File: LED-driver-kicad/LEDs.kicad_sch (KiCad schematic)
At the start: 13 parts, among them Q1 2N7002K, U2 MIC3205YML-TR

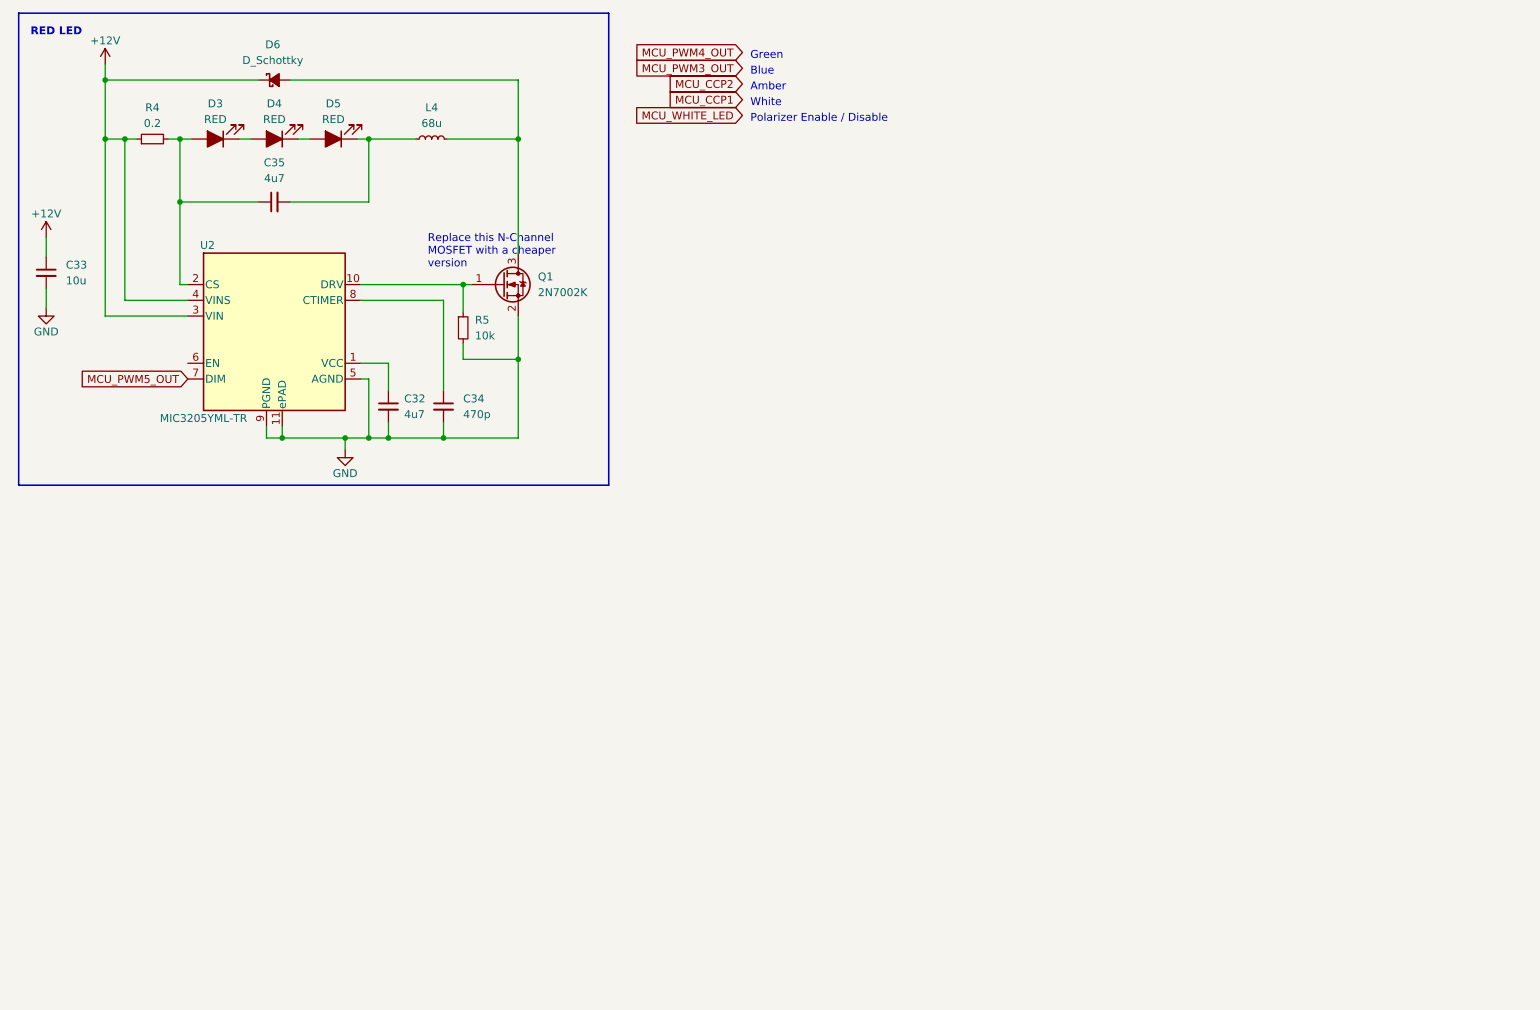
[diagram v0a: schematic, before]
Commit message: update RGB LED driver circuits
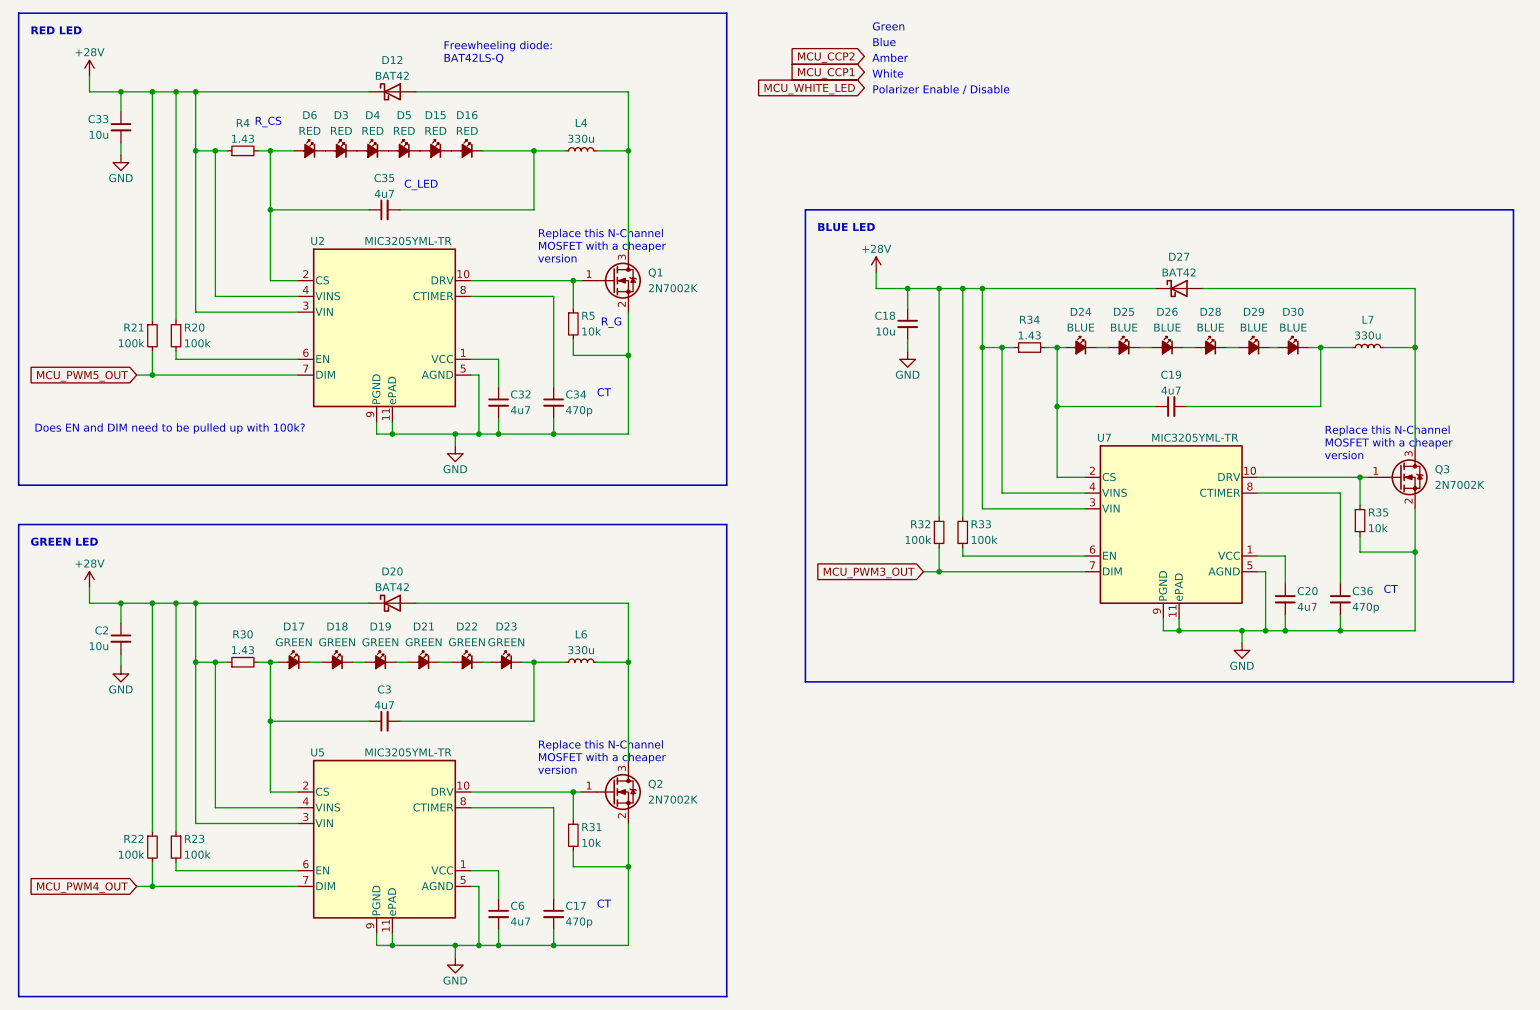
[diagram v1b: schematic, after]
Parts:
- removed D3, D4, D5: RED, symbol Device:LED_Filled
- removed D6: D_Schottky, symbol Device:D_Schottky_Small_Filled
- added C17, C36: 470p, symbol Device:C_Small
- added C18, C2: 10u, symbol Device:C_Small
- added C19, C20, C3, C6: 4u7, symbol Device:C_Small
- added D12, D20, D27: BAT42, Diode_THT:D_DO-35_SOD27_P7.62mm_Horizontal, symbol Diode:BAT42
- added D15, D16, D3, D4, D5, D6: RED, symbol Device:LED_Small_Filled
- added D17, D18, D19, D21, D22, D23: GREEN, symbol Device:LED_Small_Filled
- added D24, D25, D26, D28, D29, D30: BLUE, symbol Device:LED_Small_Filled
- added L6, L7: 330u, symbol Device:L_Small
- added Q2, Q3: 2N7002K, Package_TO_SOT_SMD:SOT-23, symbol Transistor_FET:2N7002K
- added R20, R21, R22, R23, R32, R33: 100k, symbol Device:R_Small
- added R30, R34: 1.43, symbol Device:R_Small
- added R31, R35: 10k, symbol Device:R_Small
- added U5, U7: MIC3205YML-TR, Mahabeer-Package_DFN_QFN:MLF-10_ML_MCH-Driver_LED_Microchip_MIC3205YML-TR, symbol Driver_LED_Microchip_MIC3205YML-TR:MIC3205YML-TR
- L4: value 68u -> 330u
- R4: value 0.2 -> 1.43
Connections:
- net GND: now also C17.2, C18.2, C2.2, C20.2, C36.2, C6.2, Q2.2 (S), Q3.2 (S), R31.2, R35.2, U5.11 (ePAD), U5.5 (AGND), U5.9 (PGND), U7.11 (ePAD), U7.5 (AGND), U7.9 (PGND)
- net MCU_PWM3_OUT: now also R32.2, U7.7 (DIM)
- net MCU_PWM4_OUT: now also R22.2, U5.7 (DIM)
- net MCU_PWM5_OUT: now also R21.2
- net at C35.1, R4.2, U2.2 (CS): now also D6.2 (A)
- net at C35.2, L4.1: now also D16.1 (K)
- net at L4.2, Q1.3 (D): now also D12.2 (A)
- net at U2.6 (EN): now also R20.2
- net +12V renamed +28V
- net +28V: now also C18.1, C2.1, D12.1 (K), D20.1 (K), D27.1 (K), R20.1, R21.1, R22.1, R23.1, R30.1, R32.1, R33.1, R34.1, U5.3 (VIN), U5.4 (VINS), U7.3 (VIN), U7.4 (VINS)
- new net: R23.2, U5.6 (EN)
- new net: C20.1, U7.1 (VCC)
- new net: Q3.1 (G), R35.1, U7.10 (DRV)
- new net: C19.1, D24.2 (A), R34.2, U7.2 (CS)
- new net: R33.2, U7.6 (EN)
- new net: C36.1, U7.8 (CTIMER)
- new net: D27.2 (A), L7.2, Q3.3 (D)
- new net: D28.1 (K), D29.2 (A)
- new net: D26.1 (K), D28.2 (A)
- new net: C3.1, D17.2 (A), R30.2, U5.2 (CS)
- new net: C3.2, D23.1 (K), L6.1
- new net: C6.1, U5.1 (VCC)
- new net: Q2.1 (G), R31.1, U5.10 (DRV)
- new net: C17.1, U5.8 (CTIMER)
- new net: D20.2 (A), L6.2, Q2.3 (D)
- new net: D29.1 (K), D30.2 (A)
- new net: D18.1 (K), D19.2 (A)
- new net: D17.1 (K), D18.2 (A)
- new net: D15.1 (K), D16.2 (A)
- new net: D15.2 (A), D5.1 (K)
- new net: D4.1 (K), D5.2 (A)
- new net: D3.1 (K), D4.2 (A)
- new net: C19.2, D30.1 (K), L7.1
- new net: D3.2 (A), D6.1 (K)
- new net: D21.1 (K), D22.2 (A)
- new net: D19.1 (K), D21.2 (A)
- new net: D22.1 (K), D23.2 (A)
- new net: D24.1 (K), D25.2 (A)
- new net: D25.1 (K), D26.2 (A)
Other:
- note added: "BLUE LED"
- note added: "CT"
- note added: "C_LED"
- note added: "Does EN and DIM need to be pulled up with 100k?"
- note added: "Freewheeling diode: BAT42LS-Q"
- note added: "GREEN LED"
- note added: "R_CS"
- note added: "R_G"
- moved on the sheet: C32, C33, C34, C35, L4, Q1, R4, R5, U2

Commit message: update RGB LEDs
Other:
- note added: "Blue LED"
- note added: "Green LED"
- note added: "Red LED"
- note removed: "Amber"
- note removed: "BLUE LED"
- note removed: "Blue"
- note removed: "GREEN LED"
- note removed: "Green"
- note removed: "Polarizer Enable / Disable"
- note removed: "RED LED"
- note removed: "White"
